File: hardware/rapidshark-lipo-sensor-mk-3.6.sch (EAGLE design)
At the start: 26 parts, among them Q1 IRLML2244, Q2 IRLML2502, Q3 IRLML2244, Q4 IRLML2502, Q5 IRLML2244, Q6 IRLML2502, U1 Tiny84

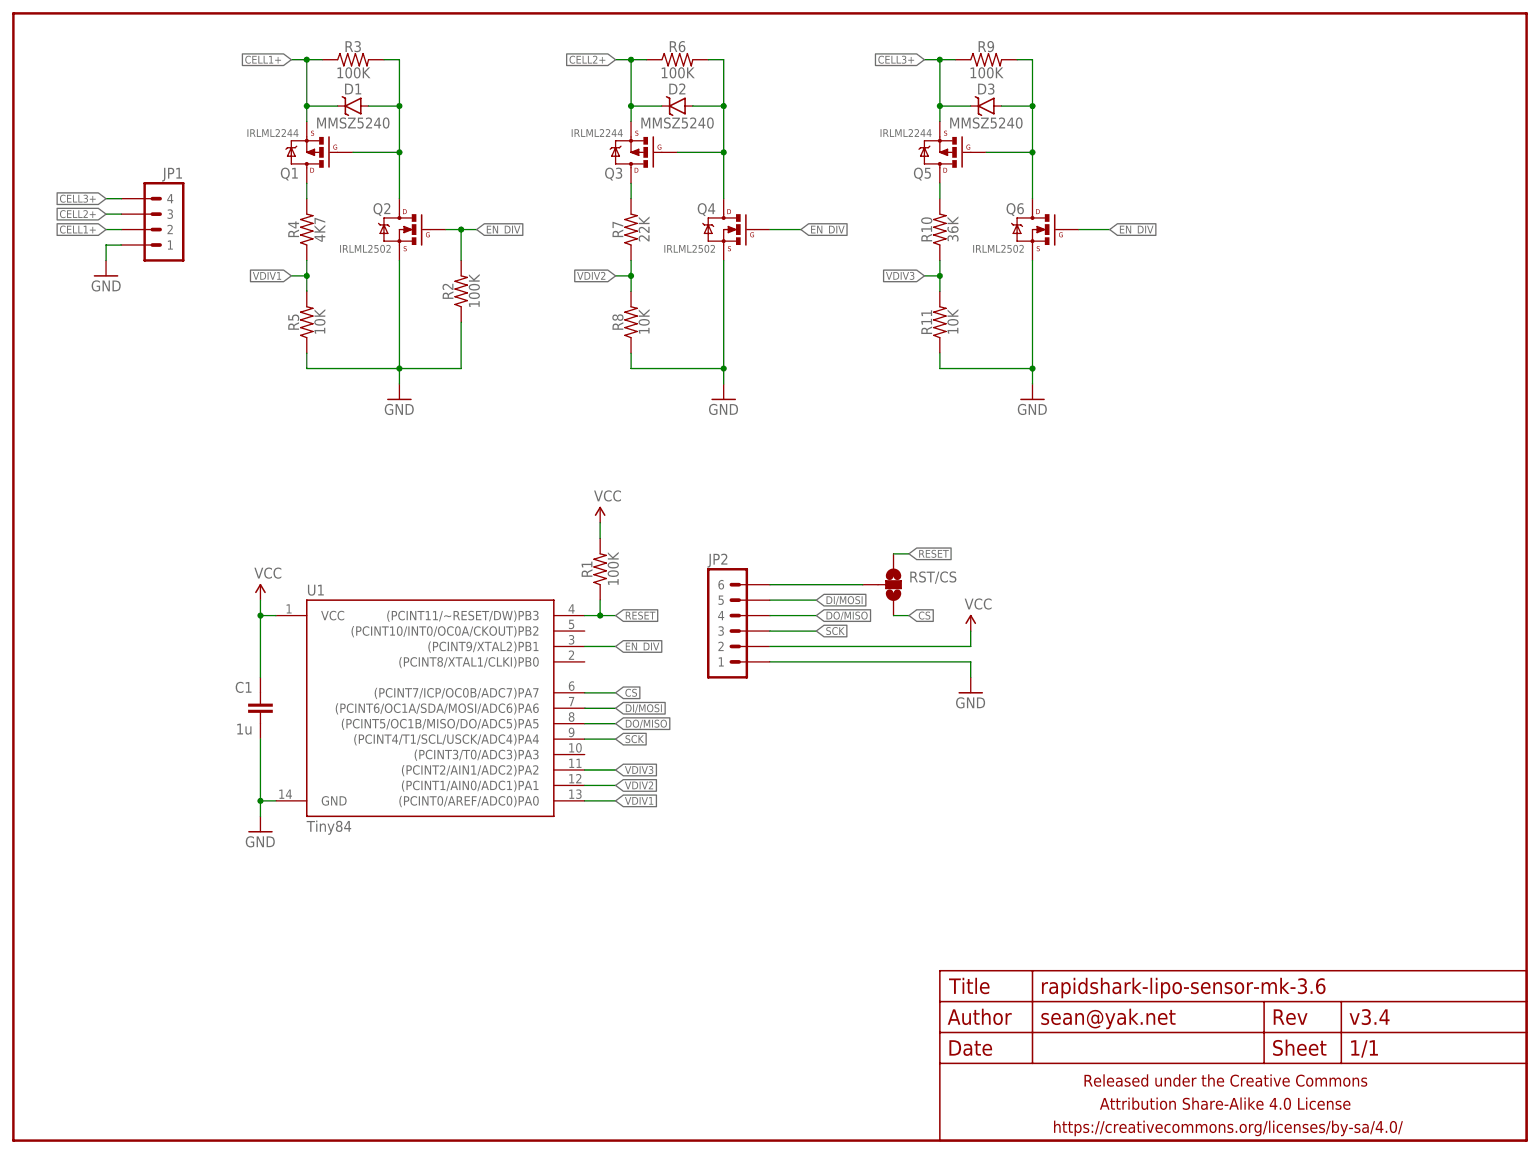
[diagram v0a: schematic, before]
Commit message: lipo sensors suck
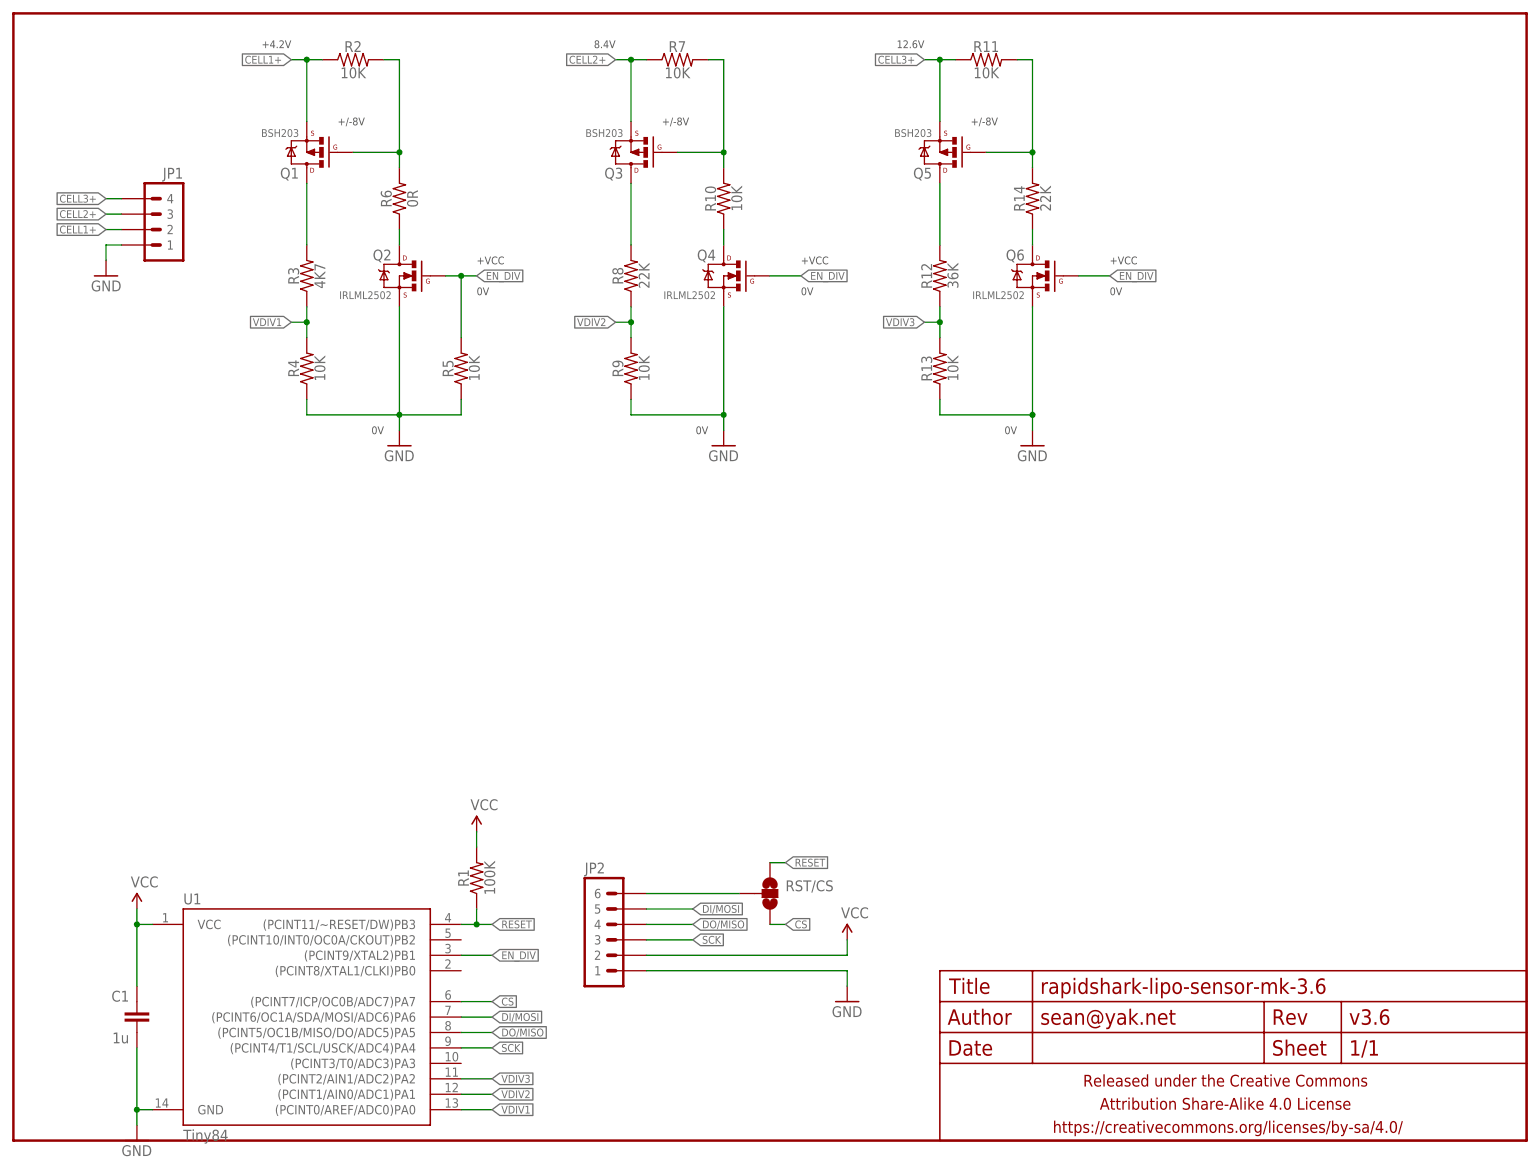
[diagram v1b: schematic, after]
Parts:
- removed D1, D2, D3: MMSZ5240, a_parts:DIODE-ZENERSOD123
- added R12: 36K, a_parts:RESISTORR0603-TIGHTER
- added R13: 10K, a_parts:RESISTORR0603-TIGHTER
- added R14: 22K, a_parts:RESISTORR0603-TIGHTER
- FRAME1: VERSION v3.4 -> v3.6
- Q1, Q3, Q5: value IRLML2244 -> BSH203
- R10: value 36K -> 10K
- R2, R9: value 100K -> 10K
- R3: value 100K -> 4K7
- R4: value 4K7 -> 10K
- R6: value 100K -> 0R
- R7: value 22K -> 10K
- R8: value 10K -> 22K
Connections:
- new net N$1: Q4.D, R10.1
- new net N$8: Q6.D, R14.1
- new net N$9: Q2.D, R6.1
- net CELL1+: now also R2.1; no longer D1.C, R3.1
- net CELL2+: now also R7.1; no longer D2.C, R6.1
- net CELL3+: now also R11.1; no longer D3.C, R9.1
- net EN_DIV: now also R5.2; no longer R2.2
- net GND: now also R13.1, R4.1, R9.1; no longer R11.1, R2.1, R8.1
- net N$2: now also R8.2; no longer R7.2
- net N$3: now also R12.2; no longer R10.2
- net N$4: now also R2.2, R6.2; no longer D1.A, Q2.D, R3.2
- net N$5: now also R10.2, R7.2; no longer D2.A, Q4.D, R6.2
- net N$6: now also R3.2; no longer R4.2
- net N$7: now also R11.2, R14.2; no longer D3.A, Q6.D, R9.2
- net VDIV1: now also R3.1, R4.2; no longer R4.1, R5.2
- net VDIV2: now also R8.1, R9.2; no longer R7.1, R8.2
- net VDIV3: now also R12.1, R13.2; no longer R10.1, R11.2
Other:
- note added: "+/-8V"
- note added: "+4.2V"
- note added: "+VCC"
- note added: "0V"
- note added: "12.6V"
- note added: "8.4V"
- moved on the sheet: C1, JP2, Q2, Q4, Q6, R1, R10, R11, R2, R3, R4, R5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
